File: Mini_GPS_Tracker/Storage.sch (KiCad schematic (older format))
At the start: 1 part, among them U8 W25Q128JVS

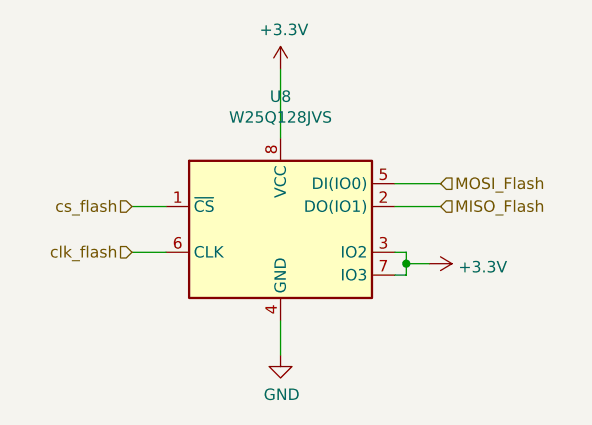
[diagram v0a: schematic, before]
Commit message: Add files via upload
 STM32F413xG/H  Chip changes
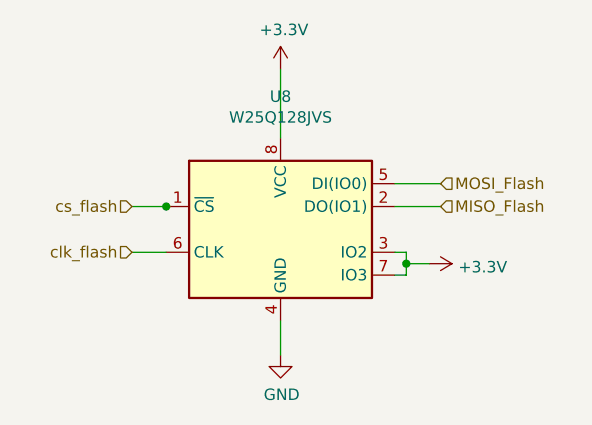
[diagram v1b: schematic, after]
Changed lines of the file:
@@
 $Descr A4 11693 8268
 encoding utf-8
-Sheet 6 6
+Sheet 6 11
 Title ""
 Date ""
@@
 Wire Wire Line
 	6200 3700 6400 3700
+Connection ~ 5200 3800
 $EndSCHEMATC
